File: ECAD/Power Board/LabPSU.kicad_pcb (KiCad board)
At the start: 2 copper layers, 93 parts, among them J1 PWR, J2 CTRL, J3 UPDI, J4 +, J5 -, Q1 Si7148DP, Q2 Si7148DP, U1 LM1117-5.0, U10 LM358, U11 ATtiny414-SS, U12 MCP4811, U13 INA286, U2 LM1117-3.3, U3 MCP4811, U4 INA180A3, U5 LM358, U6 TXB0104D, U7 MCP3204, U8 LM5118MH, U9 MCP4812

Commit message: stuff
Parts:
- moved L1 94.3 mm to (200.7, 125.7)
- moved J5 93.1 mm to (238.8, 92.7)
- moved J4 81.5 mm to (238.8, 69.8)
- moved U8 48.9 mm to (170.2, 124.5)
- moved J1 39.7 mm to (101.6, 108.0), turned to 180 degrees

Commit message: start routing
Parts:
- removed C36: 1uF, Capacitor_SMD:C_0805_2012Metric
- removed D1: V30DM60CL, footprints:TO-263AC-3
- C28, C30: value 47uF -> 22uF; footprint Capacitor_SMD:C_1812_4532Metric -> Capacitor_SMD:C_2220_5650Metric
- moved C14 136.6 mm to (69.8, 89.4)
- moved C9 132.5 mm to (69.8, 94.5)
- moved C11 128.1 mm to (69.8, 97.0)
- moved C20 128.0 mm to (69.8, 91.9)
- moved R4 122.3 mm to (87.1, 91.9), turned to 270 degrees
- moved C17 121.5 mm to (90.4, 92.5), turned to 270 degrees
- moved L1 115.9 mm to (97.8, 72.4)
- moved R6 108.7 mm to (89.2, 99.6), turned to 180 degrees
- moved Q1 101.7 mm to (67.3, 83.8), turned to 270 degrees
- moved C33 100.5 mm to (96.5, 99.6)
- moved C28 94.8 mm to (117.6, 94.2), turned to 180 degrees
- moved R5 94.5 mm to (89.2, 88.1), turned to 270 degrees
- moved C13 93.3 mm to (87.4, 95.0), turned to 180 degrees
- moved J2 90.7 mm to (148.6, 142.2), turned to 270 degrees
- moved C22 87.1 mm to (106.2, 93.7), turned to 270 degrees
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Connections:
- C33 pad 1: Net-(C28-Pad1) -> VOUT
- J1 pad 2: Net-(D1-Pad2) -> VBUS

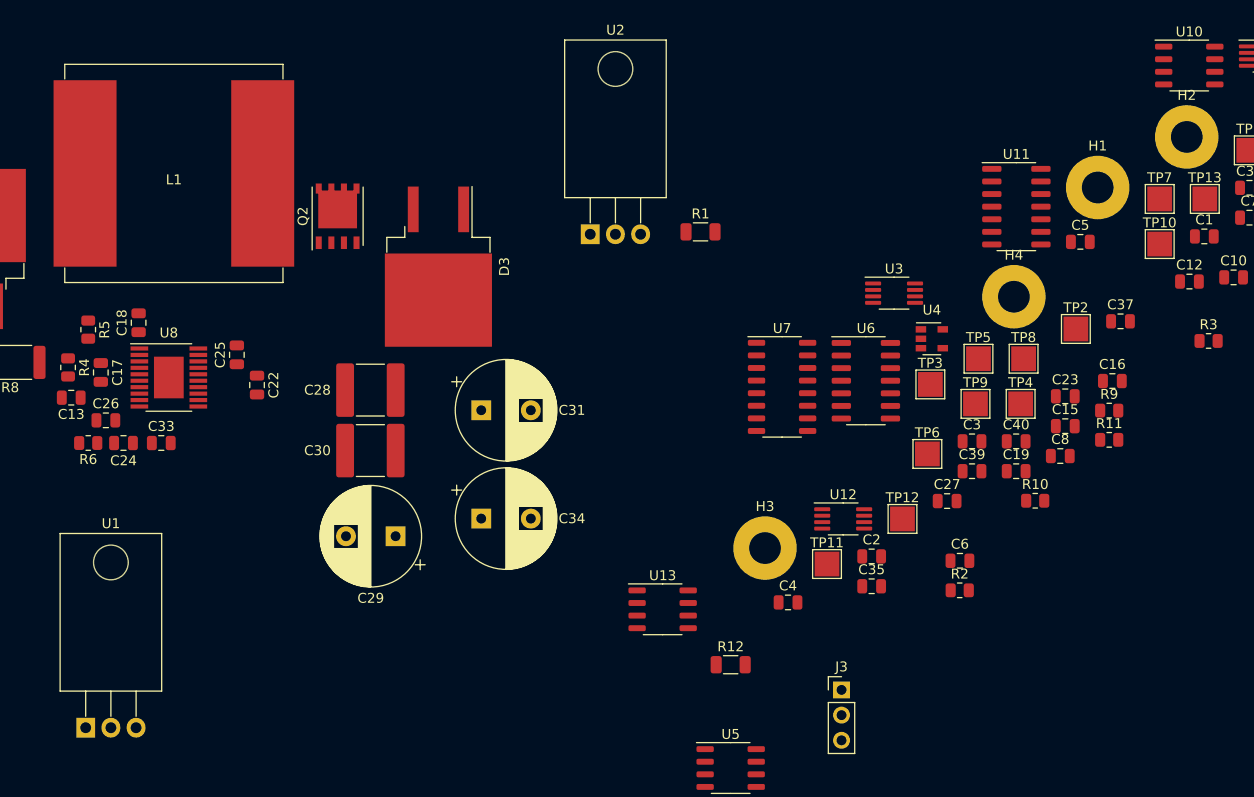
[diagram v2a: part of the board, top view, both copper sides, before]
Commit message: Implement LM317
#2
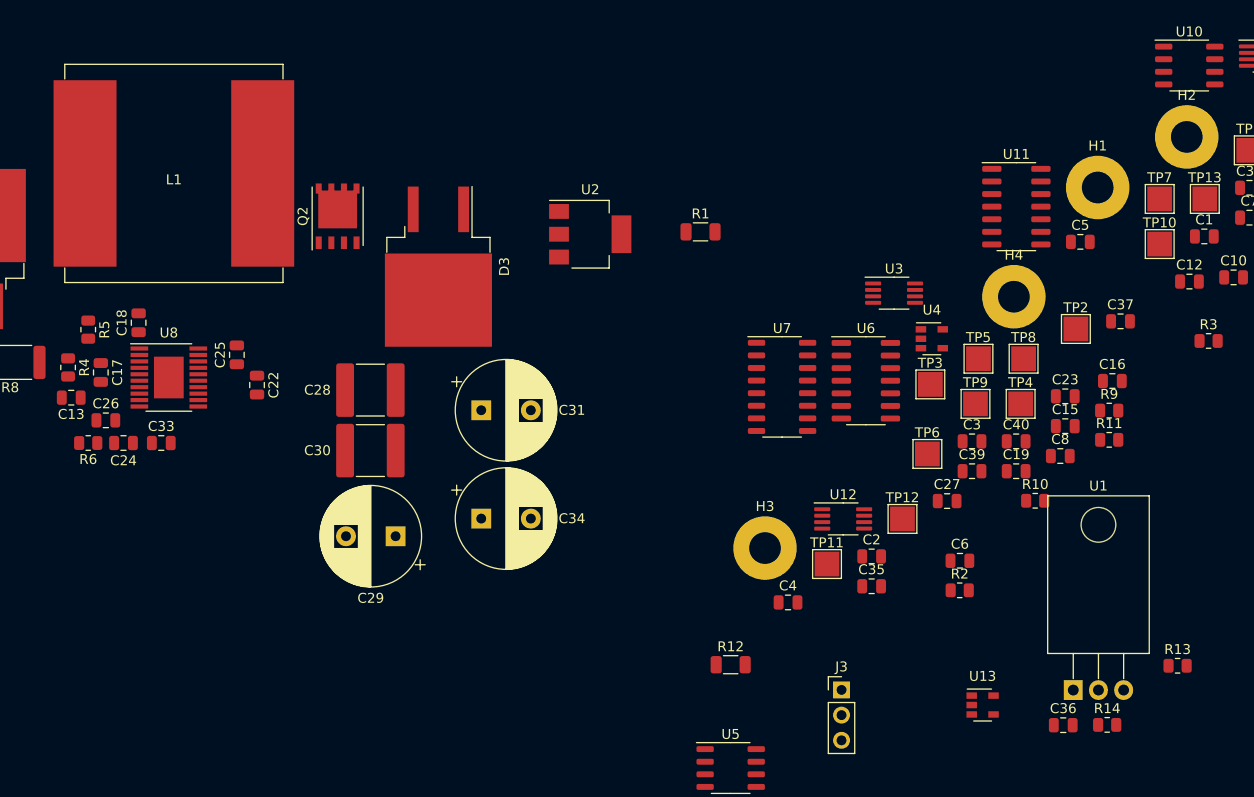
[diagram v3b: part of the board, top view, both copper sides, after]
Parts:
- added C36: 1uF, Capacitor_SMD:C_0805_2012Metric, F.Cu at (187.5, 128.0)
- added R13: 3K, Resistor_SMD:R_0805_2012Metric, F.Cu at (199.0, 122.0)
- added R14: 1K, Resistor_SMD:R_0805_2012Metric, F.Cu at (191.9, 128.0)
- C5: value 10uF -> 1uF
- U1: value LM1117-5.0 -> LM317_TO-220
- U13: value INA286 -> INA180A3; footprint Package_SO:SO-8_3.9x4.9mm_P1.27mm -> Package_TO_SOT_SMD:SOT-23-5
- U2: footprint Package_TO_SOT_THT:TO-220-3_Horizontal_TabDown -> Package_TO_SOT_SMD:SOT-223-3_TabPin2
- moved U1 99.6 mm to (188.5, 124.5)
- moved U13 33.7 mm to (179.3, 126.0)
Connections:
- C4 pad 1: VBUS -> +5V
- U1 pad 1: GND -> Net-(C36-Pad1)
- U13 pad 1: VOUT -> IOUT
- U13 pad 3: GND -> Net-(C28-Pad1)
- U13 pad 4: (no net) -> VOUT
- U13 pad 5: IOUT -> +5V
- U2 pad 3: VBUS -> +5V

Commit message: arrange components
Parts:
- removed C12: 10uF, Capacitor_SMD:C_0805_2012Metric
- removed C15: 0.1uF, Capacitor_SMD:C_0805_2012Metric
- removed U7: MCP3204, Package_SO:SO-16_3.9x9.9mm_P1.27mm
- moved TP1 153.5 mm to (53.6, 86.6)
- moved R3 143.8 mm to (58.4, 94.7), turned to 270 degrees
- moved C7 143.4 mm to (62.9, 79.2), turned to 90 degrees
- moved C21 140.2 mm to (77.1, 114.8), turned to 180 degrees
- moved U9 138.7 mm to (82.4, 119.3)
- moved C1 137.9 mm to (65.5, 101.0)
- moved TP4 125.8 mm to (58.7, 77.7)
- moved TP7 121.1 mm to (78.1, 97.2)
- moved H1 121.0 mm to (71.4, 54.9)
- moved TP6 120.9 mm to (53.0, 96.1)
- moved R2 120.9 mm to (58.4, 91.2), turned to 270 degrees
- moved C8 119.7 mm to (76.7, 54.9)
- moved C32 115.0 mm to (98.7, 114.5)
- moved C10 114.7 mm to (111.8, 150.2)
- moved U4 114.5 mm to (59.8, 83.3)
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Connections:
- U11 pad 12: /MISO -> (no net)
- U11 pad 2: /CS0 -> /VOUTSET
- U11 pad 3: /LDAC -> /IOUTSET
- U11 pad 4: /CS1 -> VOUTBUF
- U11 pad 5: (no net) -> IOUTBUF
- U11 pad 6: (no net) -> /CS0
- U11 pad 7: (no net) -> /LDAC

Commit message: start routing
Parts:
- moved J3 59.2 mm to (105.9, 122.4)
- moved C16 16.3 mm to (133.1, 151.9)
- moved C10 8.25 mm to (119.9, 151.6)
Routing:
- net Net-(C36-Pad1): track 0.00 -> 8.89 mm
- net Net-(C38-Pad1): track 0.00 -> 4.51 mm
- net Net-(C8-Pad1): track 0.00 -> 4.38 mm
- net Net-(C39-Pad1): track 0.00 -> 4.38 mm
- net Net-(C40-Pad1): track 0.00 -> 4.38 mm
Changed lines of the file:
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@@
-(kicad_pcb (version 20171130) (host pcbnew "(5.1.9)-1")
+(kicad_pcb (version 20171130) (host pcbnew "(5.1.10)-1")
   (general
     (thickness 1.6)
     (drawings 0)
-    (tracks 0)
+    (tracks 9)
     (zones 0)
     (modules 91)
@@
   )
   (setup
-    (last_trace_width 0.25)
+    (last_trace_width 0.508)
     (user_trace_width 0.254)
     (user_trace_width 0.381)
@@
   )
   (module Connector_PinHeader_2.54mm:PinHeader_1x03_P2.54mm_Vertical (layer F.Cu)
-    (at 165.1 124.46)
+    (at 105.918 122.428)
     (descr "Through hole straight pin header, 1x03, 2.54mm pitch, single row")
     (tags "Through hole pin header THT 1x03 2.54mm single row")
@@
   )
   (module Capacitor_SMD:C_0805_2012Metric (layer F.Cu)
-    (at 117.095 148.692)
+    (at 133.096 151.892)
     (descr "Capacitor SMD 0805 (2012 Metric), square (rectangular) end terminal, IPC_7351 nominal, (Body size source: IPC-SM-782 page 76, https://www.pcb-3d.com/wordpress/wp-content/uploads/ipc-sm-782a_amendment_1_and_2.pdf, https://docs.google.com/spreadsheets/d/1BsfQQcO9C6DZCsRaXUlFlo91Tg2WpOkGARC1WS5S8t0/edit?usp=sharing), generated with kicad-footprint-generator")
     (tags capacitor)
@@
   )
   (module Capacitor_SMD:C_0805_2012Metric (layer F.Cu)
-    (at 111.76 150.241)
+    (at 119.888 151.638)
     (descr "Capacitor SMD 0805 (2012 Metric), square (rectangular) end terminal, IPC_7351 nominal, (Body size source: IPC-SM-782 page 76, https://www.pcb-3d.com/wordpress/wp-content/uploads/ipc-sm-782a_amendment_1_and_2.pdf, https://docs.google.com/spreadsheets/d/1BsfQQcO9C6DZCsRaXUlFlo91Tg2WpOkGARC1WS5S8t0/edit?usp=sharing), generated with kicad-footprint-generator")
     (tags capacitor)
@@
     )
   )
+  (segment (start 75.758 54.864) (end 71.374 54.864) (width 1.27) (layer F.Cu) (net 5))
+  (segment (start 165.161 70.993) (end 169.672 70.993) (width 1.27) (layer F.Cu) (net 16))
+  (segment (start 88.712 141.859) (end 84.328 141.859) (width 1.27) (layer F.Cu) (net 17))
+  (segment (start 167.574 151.765) (end 171.958 151.765) (width 1.27) (layer F.Cu) (net 18))
+  (segment (start 149.5025 118.999) (end 151.2335 118.999) (width 0.508) (layer F.Cu) (net 53))
+  (segment (start 151.124 118.8895) (end 151.2335 118.999) (width 0.508) (layer F.Cu) (net 53))
+  (segment (start 151.124 115.205) (end 151.124 118.8895) (width 0.508) (layer F.Cu) (net 53))
+  (segment (start 149.54 119.0365) (end 149.5025 118.999) (width 0.508) (layer F.Cu) (net 53))
+  (segment (start 149.54 122.301) (end 149.54 119.0365) (width 0.508) (layer F.Cu) (net 53))
 )

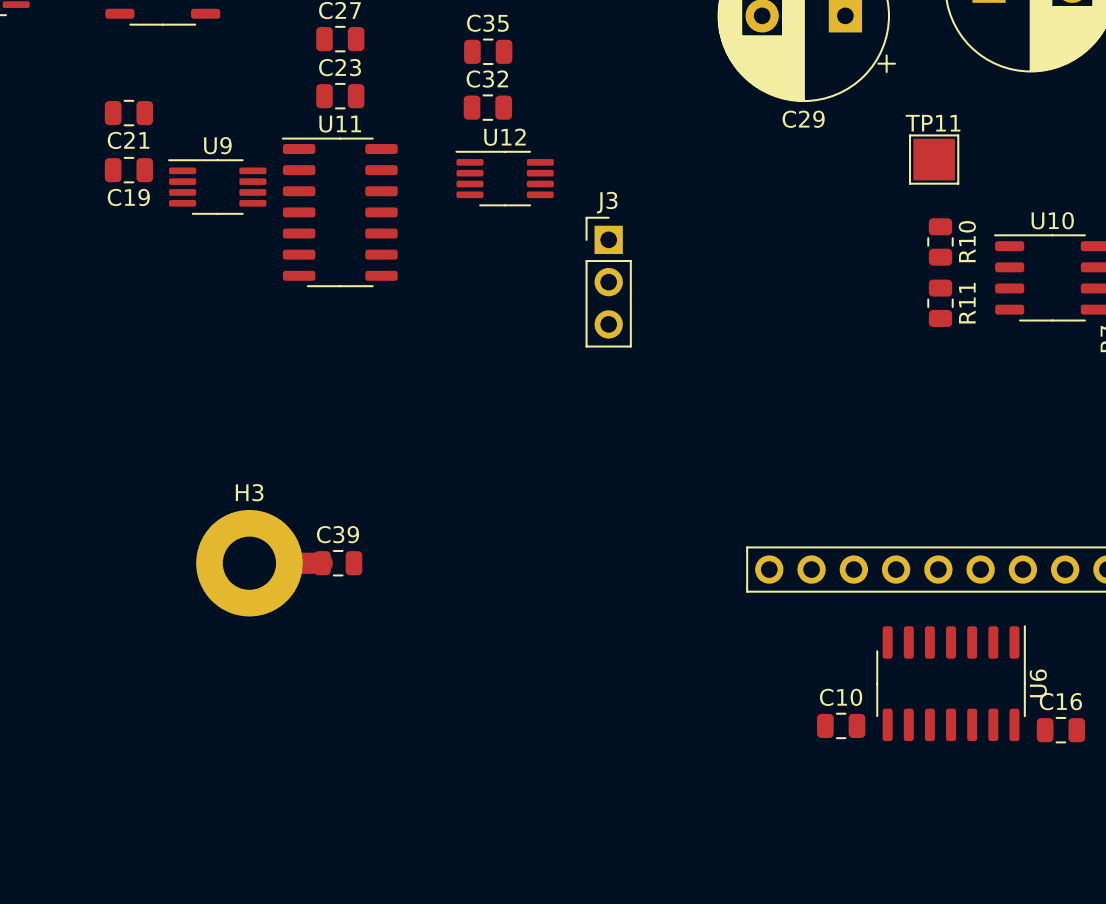
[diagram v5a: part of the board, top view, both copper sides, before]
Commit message: Switch back to i2c control
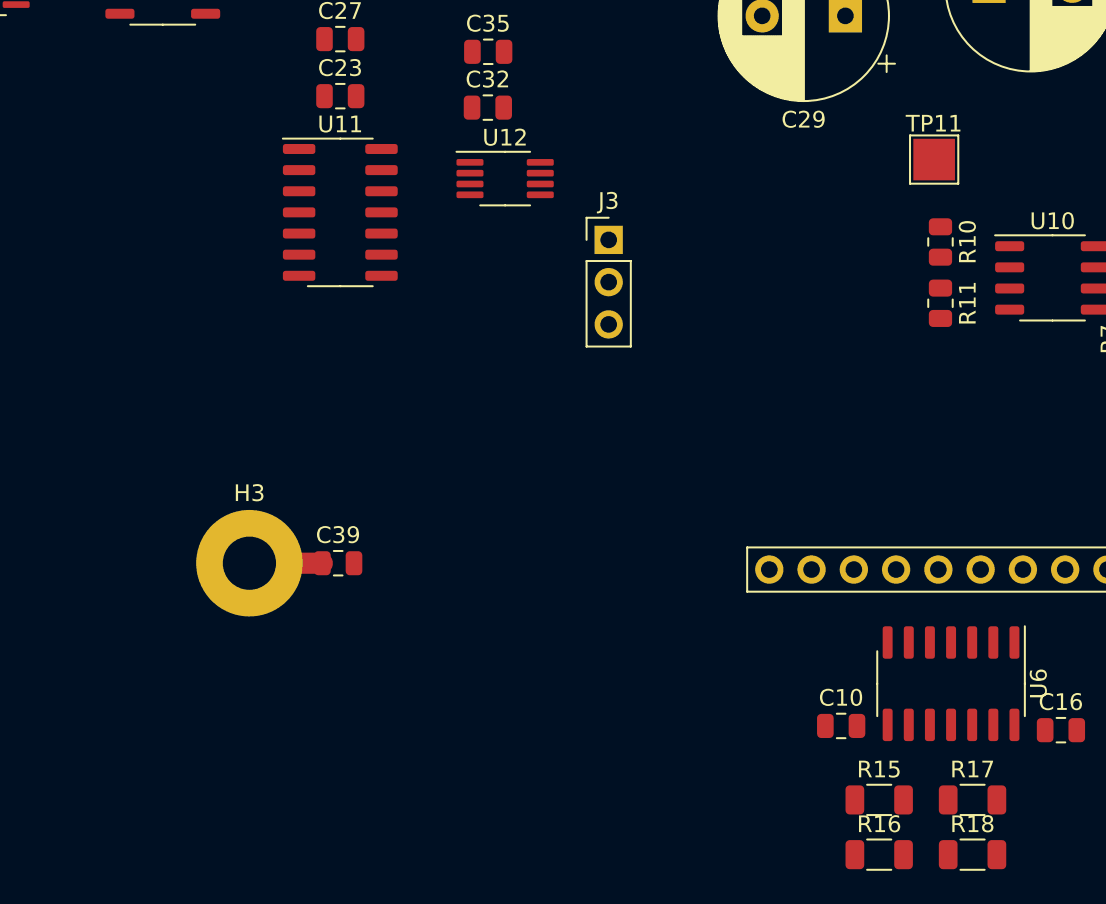
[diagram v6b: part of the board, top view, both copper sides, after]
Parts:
- removed C19: 10uF, Capacitor_SMD:C_0805_2012Metric
- removed C21: 0.1uF, Capacitor_SMD:C_0805_2012Metric
- removed U9: MCP4812, Package_SO:MSOP-8_3x3mm_P0.65mm
- added R15: 2.2K, Resistor_SMD:R_1206_3216Metric, F.Cu at (122.2, 156.1)
- added R16: 2.2K, Resistor_SMD:R_1206_3216Metric, F.Cu at (122.2, 159.4)
- added R17: 2.2K, Resistor_SMD:R_1206_3216Metric, F.Cu at (127.8, 156.1)
- added R18: 2.2K, Resistor_SMD:R_1206_3216Metric, F.Cu at (127.8, 159.4)
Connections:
- J2 pad 10: M_CS0 -> M_CS1
- J2 pad 11: M_CS1 -> M_LDAC1
- J2 pad 12: M_LDAC0 -> SCL_SH
- J2 pad 13: M_LDAC1 -> SDA_SH
- U11 pad 2: /VOUTSET -> /CS0
- U11 pad 3: /IOUTSET -> /LDAC
- U11 pad 6: /CS0 -> (no net)
- U11 pad 7: /LDAC -> (no net)
- U11 pad 8: (no net) -> SDA
- U11 pad 9: (no net) -> SCL
- U6 pad 10: Net-(U6-Pad10) -> (no net)
- U6 pad 11: Net-(U6-Pad11) -> (no net)
- U6 pad 12: Net-(U6-Pad12) -> SDA
- U6 pad 13: Net-(U6-Pad13) -> SCL
- U6 pad 2: M_SCK -> SCL_SH
- U6 pad 3: M_MOSI -> SDA_SH
- U6 pad 4: M_CS0 -> (no net)
- U6 pad 5: M_LDAC0 -> (no net)
